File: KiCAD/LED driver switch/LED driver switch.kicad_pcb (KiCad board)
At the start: 2 copper layers, 100 x 98 mm, 37 parts, among them J2 3x Banana Jack, J3 Conn_Coaxial, J4 8P8C_Shielded, J5 Conn_01x04_Pin, Q1 PMOS, Q2 TN2124, SW1 SW_Push_LED, U1 Itsy_Bitsy_32u4, U2 4.096V

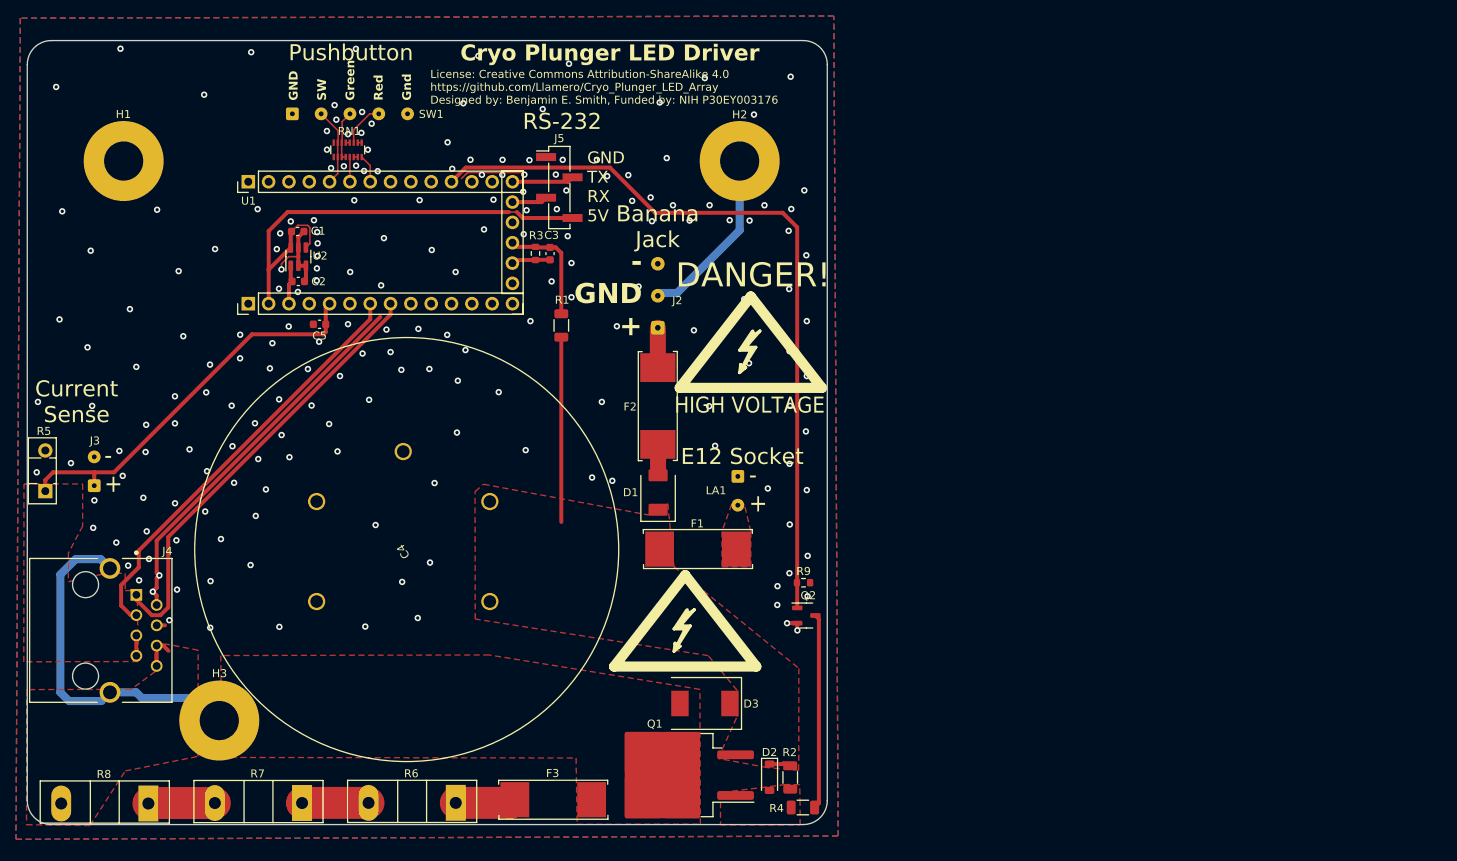
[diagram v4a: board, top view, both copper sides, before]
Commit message: Move cap and standoff, fix cap polarity, add jumper 0V to GND
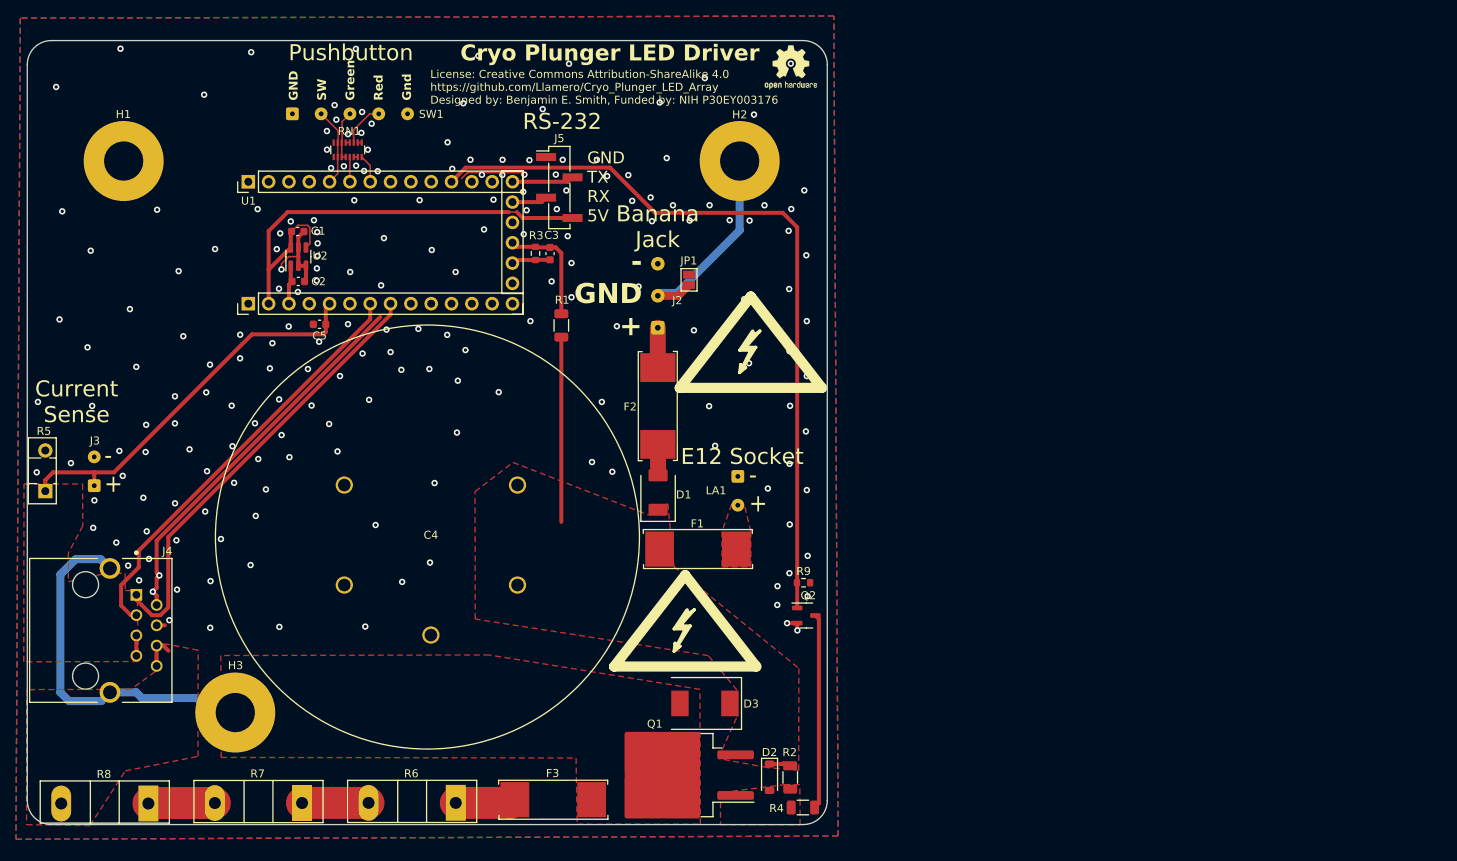
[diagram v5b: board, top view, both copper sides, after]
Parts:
- added JP1: Jumper_2_Open, Jumper:SolderJumper-2_P1.3mm_Open_Pad1.0x1.5mm, F.Cu at (102.7, 46.9)
- added SYM3: Logo_Open_Hardware_Small, Symbol:OSHW-Logo2_7.3x6mm_SilkScreen, F.Cu at (115.5, 20.4)
- moved C4 29.0 mm to (81.3, 72.6), turned to -60 degrees
- moved SYM1 3.48 mm to (70.3, 80.5), turned to 0 degrees
- moved H3 2.24 mm to (46.0, 100.9)
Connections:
- C4 pad 1: GND -> /0-200V
- C4 pad 2: GND -> /0-200V
- C4 pad 3: /0-200V -> GND
- C4 pad 4: /0-200V -> GND
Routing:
- net Earth_Protective: track 66.6 -> 71.0 mm
- net GND: vias 198 -> 196

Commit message: Move high voltage away from board edge - build enclosure model
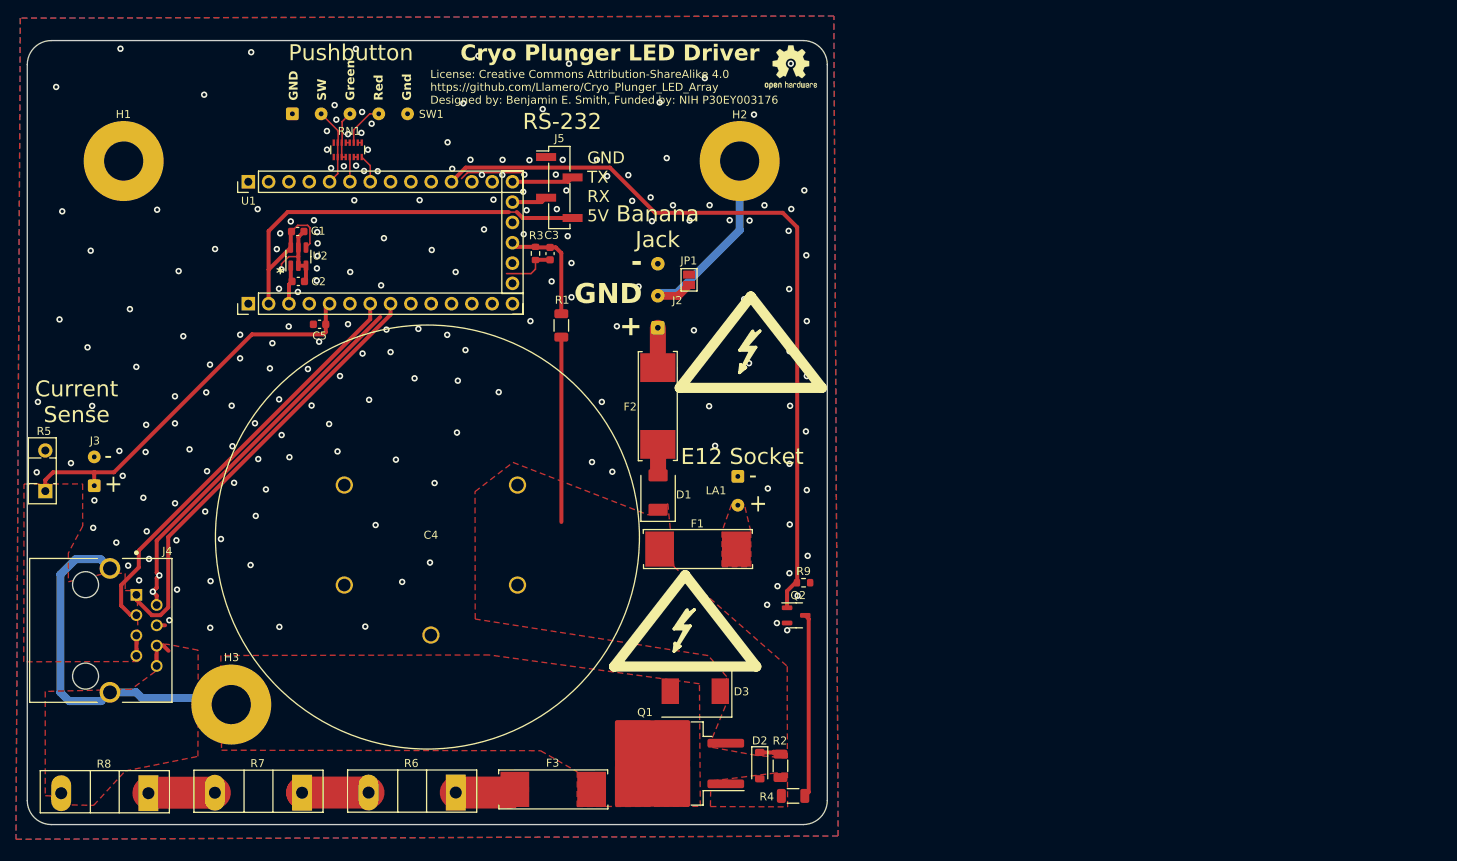
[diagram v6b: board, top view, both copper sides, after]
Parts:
- moved D3 1.95 mm to (103.5, 98.3)
- moved R2 1.90 mm to (114.1, 107.7)
- moved R4 1.90 mm to (115.7, 111.4)
- moved D2 1.90 mm to (111.6, 107.6)
- moved Q1 1.90 mm to (99.7, 107.4)
- moved F3 1.29 mm to (85.2, 110.6)
- moved R6 1.29 mm to (73.6, 111.0)
- moved R7 1.29 mm to (54.4, 111.0)
- moved R8 1.29 mm to (35.1, 111.1)
- moved Q2 1.27 mm to (116.1, 88.8)
- moved H3 1.12 mm to (45.5, 99.9)
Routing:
- net Net-(Q2-D): track 24.4 -> 23.0 mm
- net /LED_trigger: track 94.6 -> 95.2 mm
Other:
- board text added: "*"

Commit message: Add high voltage slots
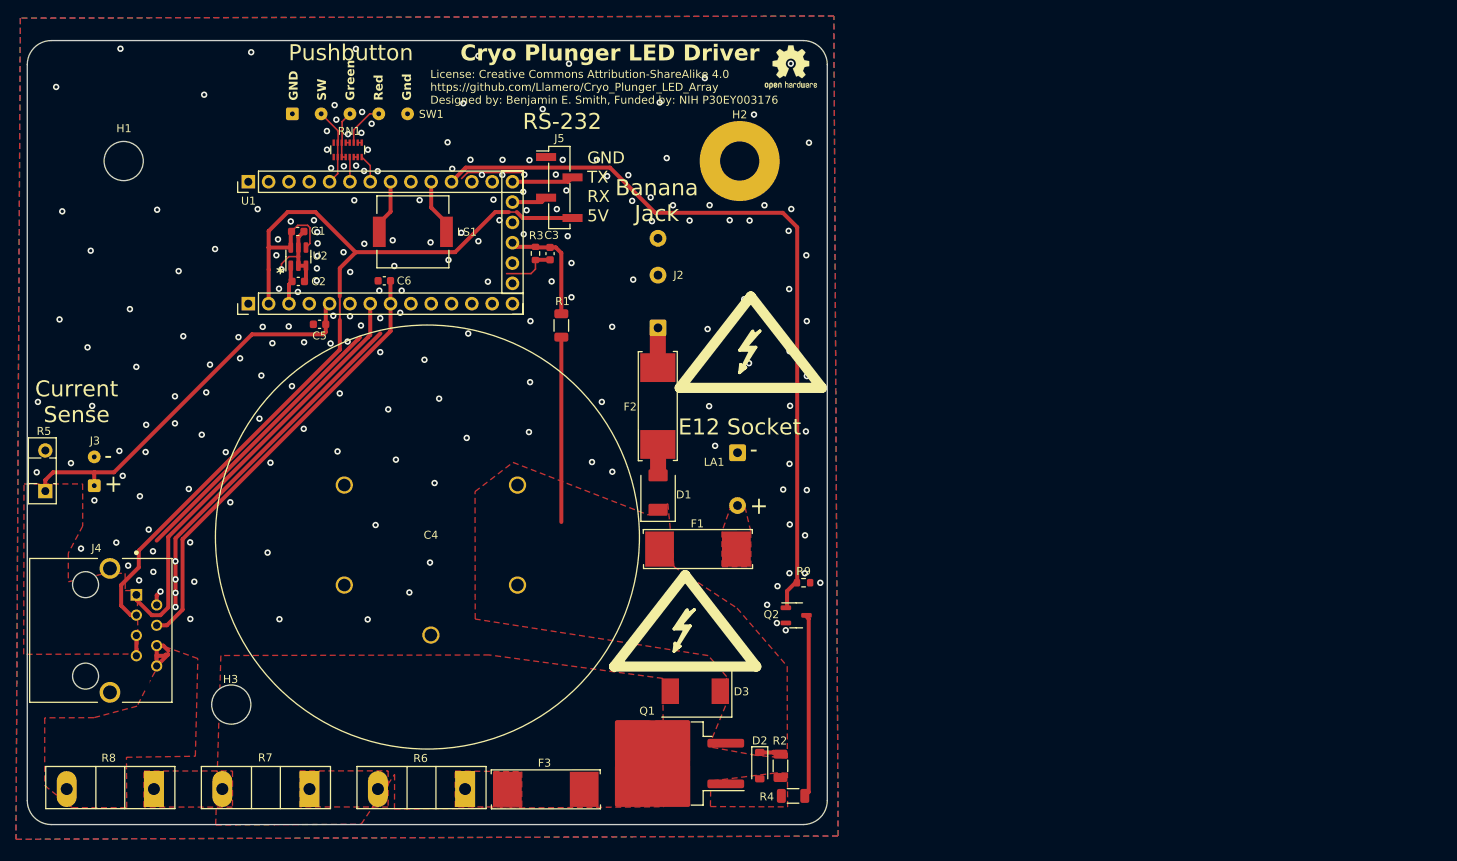
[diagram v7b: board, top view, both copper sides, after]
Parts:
- removed JP1: Jumper_2_Open, Jumper:SolderJumper-2_P1.3mm_Open_Pad1.0x1.5mm
- added C6: 1nF, Capacitor_SMD:C_0603_1608Metric, F.Cu at (64.6, 47.0)
- added LS1: Speaker_Crystal, Custom footprints:XDCR_SMT-0940-T-3V-R, F.Cu at (68.2, 40.9)
- H1, H3: footprint Custom footprints:8-32 Standoff -> Custom footprints:8-32 Isolated Hole
- J2: footprint Connector_Wire:SolderWire-0.15sqmm_1x03_P4mm_D0.5mm_OD1.5mm -> Custom footprints:SolderWire-0.5sqmm_1x03_P4.6mm_D0.9mm_OD2.1mm - HV Slot
- J4: footprint Custom footprints:BEL_SS71800-019F -> Custom footprints:BEL_SS71800-019F - HV Slot
- LA1: footprint Connector_Wire:SolderWire-0.1sqmm_1x02_P3.6mm_D0.4mm_OD1mm -> Custom footprints:SolderWire-0.5sqmm_1x02_P4.6mm_D0.9mm_OD2.1mm - HV Slot
- Q2: footprint Package_TO_SOT_SMD:SOT-23-3 -> Custom footprints:SOT-23-3 - HV Slot
- R1: footprint Resistor_SMD:R_1206_3216Metric -> Custom footprints:R_1206_3216 - HV slot
- moved LA1 2.96 mm to (108.8, 68.5)
- moved J2 1.98 mm to (98.8, 50.9)
- moved R6 1.25 mm to (74.7, 110.6)
- moved R7 1.04 mm to (55.3, 110.6)
- moved F3 0.93 mm to (84.2, 110.6)
- moved R8 0.86 mm to (35.8, 110.6)
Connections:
- H2 pad 1: Earth_Protective -> GND
- J2 pad 2: Earth_Protective -> GND
- J4 pad 3: /Trap door sensor -> +5V
- J4 pad 4: GND -> /Audio out
- J4 pad SH: Earth_Protective -> GND
- U1 pad 24: unconnected-(U1-~5-Pad24) -> Net-(U1-~5)
- U1 pad 26: unconnected-(U1-~9_A9-Pad26) -> Net-(U1-~9_A9)
- U1 pad 7: /Trap door sensor -> /Door safety interlock
- U1 pad 8: /Door safety interlock -> /Audio out
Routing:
- net Earth_Protective: track 71.0 -> 0.00 mm
- net +5V: track 59.7 -> 121.5 mm
- net /Audio out: track 0.00 -> 55.9 mm
- net /Trap door sensor: track 53.0 -> 0.00 mm
- net GND: track 75.7 -> 109.1 mm, vias 196 -> 200
- net Net-(R7-Pad2): track 8.33 -> 0.00 mm
- net Net-(R6-Pad2): track 8.32 -> 0.00 mm
- net Net-(F3-Pad1): track 7.35 -> 0.00 mm
- net Net-(U1-~5): track 0.00 -> 7.05 mm
- net Net-(U1-~9_A9): track 0.00 -> 6.84 mm
- net /LED+: track 4.28 -> 7.76 mm
- net /Door safety interlock: track 55.3 -> 54.2 mm
- added copper zone on F.Cu, net Net-(F3-Pad1)
- added copper zone on F.Cu, net Net-(R6-Pad2)
- added copper zone on F.Cu, net Net-(R7-Pad2)
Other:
- board text removed: "- GND +"

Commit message: Add label
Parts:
- moved R3 1.83 mm to (85.3, 43.6)
- moved C3 1.81 mm to (83.5, 43.6)
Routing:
- net GND: vias 200 -> 198
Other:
- board text added: "- Gnd +"
